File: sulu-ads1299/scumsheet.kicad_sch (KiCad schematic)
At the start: 16 parts, among them J11 through_hole, J16 through_hole, J17 through_hole, J20 through_hole, J4 through_hole, J5 through_hole, J6 through_hole, J8 through_hole, U5 scum3

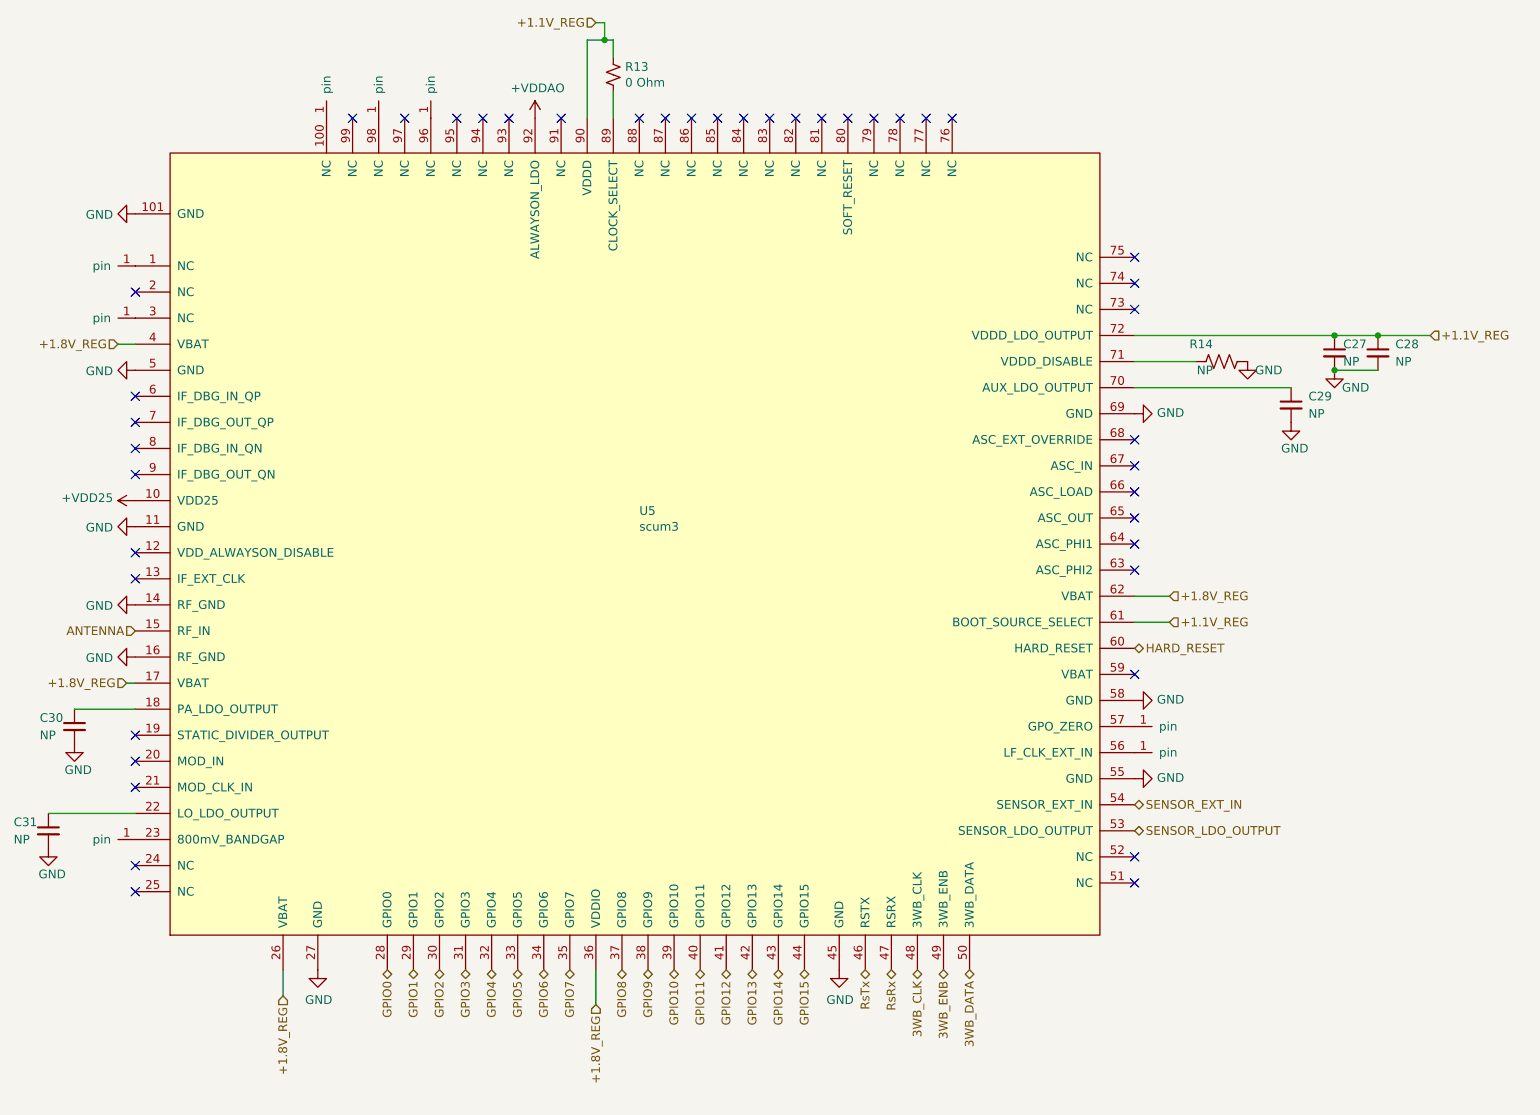
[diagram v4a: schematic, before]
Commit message: Updated connector boards and Sulu-ADS1299 schematic
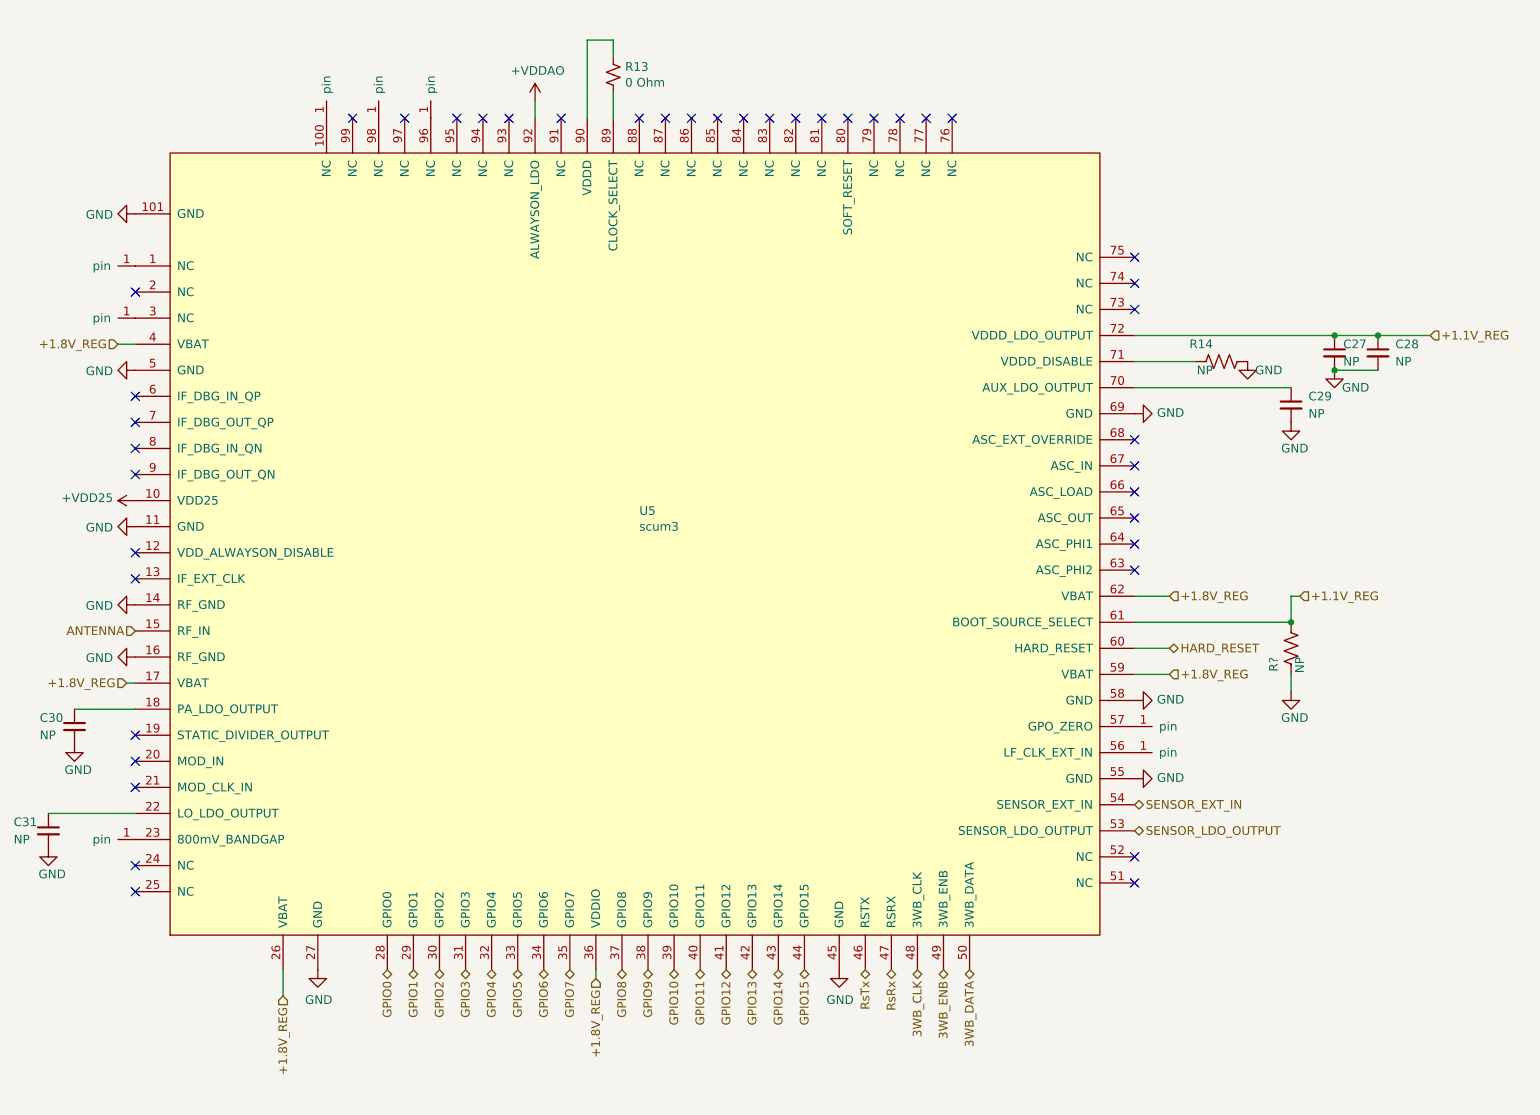
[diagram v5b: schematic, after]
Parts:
- added R?: NP, Resistor_SMD:R_0402_1005Metric, symbol Device:R_US
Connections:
- net +1.1V_REG: now also R?.2; no longer R13.1, U5.90 (VDDD)
- net +1.8V_REG: now also U5.59 (VBAT)
- net GND: now also R?.1
- new net: R13.1, U5.90 (VDDD)
- no-connect marks 43 -> 42
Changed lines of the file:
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@@
   (junction (at 245.11 60.96) (diameter 0) (color 0 0 0 0)
   )
+  (junction (at 232.41 102.87) (diameter 0) (color 0 0 0 0)
+  )
   (junction (at 238.76 60.96) (diameter 0) (color 0 0 0 0)
-  )
-  (junction (at 132.08 17.78) (diameter 0) (color 0 0 0 0)
   )
   (junction (at 238.76 66.04) (diameter 0) (color 0 0 0 0)
@@
   (no_connect (at 179.07 29.21))
   (no_connect (at 95.25 29.21))
-  (no_connect (at 209.55 110.49))
   (no_connect (at 63.5 142.24))
   (no_connect (at 209.55 57.15))
@@
   (no_connect (at 144.78 29.21))
   (no_connect (at 118.11 29.21))
+  (wire (pts (xy 233.68 99.06) (xy 232.41 99.06))
+    (stroke (width 0) (type default) (color 0 0 0 0))
+  )
   (wire (pts (xy 209.55 64.77) (xy 218.44 64.77))
     (stroke (width 0) (type default) (color 0 0 0 0))
@@
     (stroke (width 0) (type default) (color 0 0 0 0))
   )
-  (wire (pts (xy 130.81 15.24) (xy 132.08 15.24))
-    (stroke (width 0) (type default) (color 0 0 0 0))
-  )
   (wire (pts (xy 62.23 111.76) (xy 63.5 111.76))
     (stroke (width 0) (type default) (color 0 0 0 0))
   )
-  (wire (pts (xy 133.35 17.78) (xy 132.08 17.78))
-    (stroke (width 0) (type default) (color 0 0 0 0))
-  )
   (wire (pts (xy 133.35 17.78) (xy 133.35 20.32))
     (stroke (width 0) (type default) (color 0 0 0 0))
@@
     (stroke (width 0) (type default) (color 0 0 0 0))
   )
+  (wire (pts (xy 121.92 26.67) (xy 121.92 29.21))
+    (stroke (width 0) (type default) (color 0 0 0 0))
+  )
+  (wire (pts (xy 232.41 99.06) (xy 232.41 102.87))
+    (stroke (width 0) (type default) (color 0 0 0 0))
+  )
   (wire (pts (xy 50.8 130.81) (xy 63.5 130.81))
     (stroke (width 0) (type default) (color 0 0 0 0))
   )
-  (wire (pts (xy 209.55 102.87) (xy 214.63 102.87))
+  (wire (pts (xy 209.55 102.87) (xy 232.41 102.87))
+    (stroke (width 0) (type default) (color 0 0 0 0))
+  )
+  (wire (pts (xy 232.41 110.49) (xy 232.41 113.03))
     (stroke (width 0) (type default) (color 0 0 0 0))
   )
@@
     (stroke (width 0) (type default) (color 0 0 0 0))
   )
-  (wire (pts (xy 130.81 153.67) (xy 130.81 158.75))
+  (wire (pts (xy 130.81 153.67) (xy 130.81 154.94))
     (stroke (width 0) (type default) (color 0 0 0 0))
   )
@@
     (stroke (width 0) (type default) (color 0 0 0 0))
   )
+  (wire (pts (xy 209.55 110.49) (xy 214.63 110.49))
+    (stroke (width 0) (type default) (color 0 0 0 0))
+  )
   (wire (pts (xy 60.96 62.23) (xy 63.5 62.23))
     (stroke (width 0) (type default) (color 0 0 0 0))
   )
+  (wire (pts (xy 214.63 106.68) (xy 209.55 106.68))
+    (stroke (width 0) (type default) (color 0 0 0 0))
+  )
   (wire (pts (xy 129.54 29.21) (xy 129.54 17.78))
     (stroke (width 0) (type default) (color 0 0 0 0))
@@
     (stroke (width 0) (type default) (color 0 0 0 0))
   )
-  (wire (pts (xy 132.08 15.24) (xy 132.08 17.78))
-    (stroke (width 0) (type default) (color 0 0 0 0))
-  )
-  (wire (pts (xy 132.08 17.78) (xy 129.54 17.78))
+  (wire (pts (xy 129.54 17.78) (xy 133.35 17.78))
     (stroke (width 0) (type default) (color 0 0 0 0))
   )
@@
     (effects (font (size 1.27 1.27)) (justify right))
   )
-  (hierarchical_label "+1.8V_REG" (shape input) (at 130.81 158.75 270)
+  (hierarchical_label "+1.8V_REG" (shape input) (at 130.81 154.94 270)
     (effects (font (size 1.27 1.27)) (justify right))
   )
@@
     (effects (font (size 1.27 1.27)) (justify right))
   )
-  (hierarchical_label "HARD_RESET" (shape bidirectional) (at 209.55 106.68 0)
+  (hierarchical_label "HARD_RESET" (shape bidirectional) (at 214.63 106.68 0)
     (effects (font (size 1.27 1.27)) (justify left))
   )
@@
     (effects (font (size 1.27 1.27)) (justify right))
   )
+  (hierarchical_label "+1.1V_REG" (shape input) (at 233.68 99.06 0)
+    (effects (font (size 1.27 1.27)) (justify left))
+  )
   (hierarchical_label "3WB_DATA" (shape bidirectional) (at 185.42 153.67 270)
     (effects (font (size 1.27 1.27)) (justify right))
@@
     (effects (font (size 1.27 1.27)) (justify left))
   )
-  (hierarchical_label "+1.1V_REG" (shape input) (at 130.81 15.24 180)
-    (effects (font (size 1.27 1.27)) (justify right))
-  )
   (hierarchical_label "GPIO11" (shape bidirectional) (at 146.05 153.67 270)
     (effects (font (size 1.27 1.27)) (justify right))
@@
     (effects (font (size 1.27 1.27)) (justify left))
   )
-  (hierarchical_label "+1.1V_REG" (shape input) (at 214.63 102.87 0)
+  (hierarchical_label "+1.8V_REG" (shape input) (at 214.63 110.49 0)
     (effects (font (size 1.27 1.27)) (justify left))
   )
@@
     (pin "99")
   )
+  (symbol (lib_id "power:GND") (at 232.41 113.03 0) (unit 1)
+    (in_bom yes) (on_board yes)
+    (property "Reference" "#PWR?" (id 0) (at 232.41 119.38 0)
+      (effects (font (size 1.27 1.27)) hide)
+    )
+    (property "Value" "GND" (id 1) (at 234.95 116.84 0)
+      (effects (font (size 1.27 1.27)) (justify right))
+    )
+    (property "Footprint" "" (id 2) (at 232.41 113.03 0)
+      (effects (font (size 1.27 1.27)) hide)
+    )
+    (property "Datasheet" "" (id 3) (at 232.41 113.03 0)
+      (effects (font (size 1.27 1.27)) hide)
+    )
+    (pin "1")
+  )
   (symbol (lib_id "power:GND") (at 209.55 72.39 90) (unit 1)
     (in_bom yes) (on_board yes)
@@
     (pin "1")
   )
-  (symbol (lib_id "draft1library:+VDDAO") (at 121.92 29.21 0) (unit 1)
-    (in_bom yes) (on_board yes)
-    (property "Reference" "#PWR059" (id 0) (at 121.92 33.02 0)
-      (effects (font (size 1.27 1.27)) hide)
-    )
-    (property "Value" "+VDDAO" (id 1) (at 122.301 24.8158 0))
-    (property "Footprint" "" (id 2) (at 121.92 29.21 0)
-      (effects (font (size 1.27 1.27)) hide)
-    )
-    (property "Datasheet" "" (id 3) (at 121.92 29.21 0)
+  (symbol (lib_id "draft1library:+VDDAO") (at 121.92 26.67 0) (unit 1)
+    (in_bom yes) (on_board yes)
+    (property "Reference" "#PWR059" (id 0) (at 121.92 30.48 0)
+      (effects (font (size 1.27 1.27)) hide)
+    )
+    (property "Value" "+VDDAO" (id 1) (at 122.301 22.2758 0))
+    (property "Footprint" "" (id 2) (at 121.92 26.67 0)
+      (effects (font (size 1.27 1.27)) hide)
+    )
+    (property "Datasheet" "" (id 3) (at 121.92 26.67 0)
       (effects (font (size 1.27 1.27)) hide)
     )
@@
     (pin "1")
   )
+  (symbol (lib_id "Device:R_US") (at 232.41 106.68 180) (unit 1)
+    (in_bom yes) (on_board yes)
+    (property "Reference" "R?" (id 0) (at 229.87 107.95 90)
+      (effects (font (size 1.27 1.27)) (justify left))
+    )
+    (property "Value" "NP" (id 1) (at 233.68 107.95 90)
+      (effects (font (size 1.27 1.27)) (justify left))
+    )
+    (property "Footprint" "Resistor_SMD:R_0402_1005Metric" (id 2) (at 231.394 106.426 90)
+      (effects (font (size 1.27 1.27)) hide)
+    )
+    (property "Datasheet" "~" (id 3) (at 232.41 106.68 0)
+      (effects (font (size 1.27 1.27)) hide)
+    )
+    (pin "1")
+    (pin "2")
+  )
   (symbol (lib_id "draft1library:through_hole") (at 63.5 58.42 180) (unit 1)

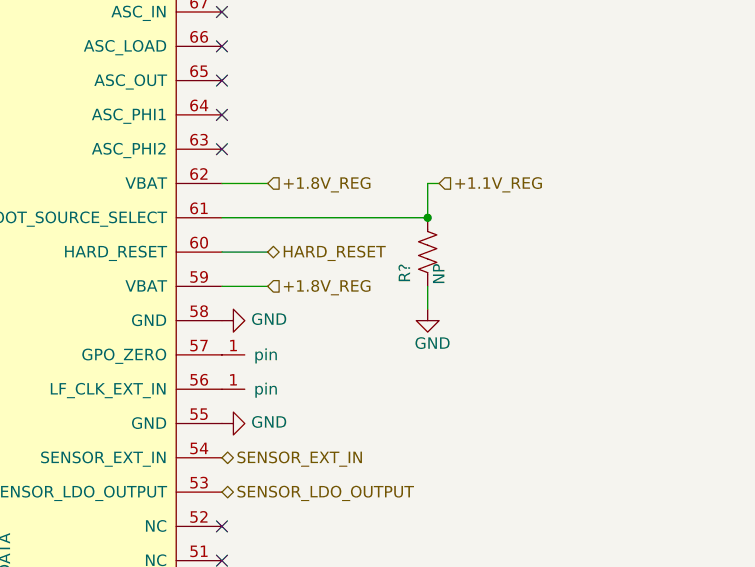
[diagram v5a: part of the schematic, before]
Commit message: Sulu-ADS1299 rev 3 fixed gpios, debug connector, two regulators
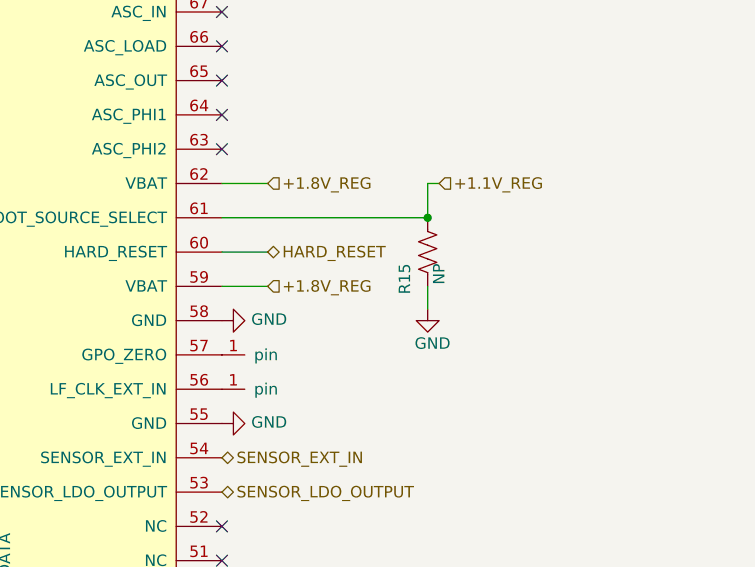
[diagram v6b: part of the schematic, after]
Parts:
- gave numbers to parts that had none: 1
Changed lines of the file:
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@@
   (symbol (lib_id "power:GND") (at 232.41 113.03 0) (unit 1)
     (in_bom yes) (on_board yes)
-    (property "Reference" "#PWR?" (id 0) (at 232.41 119.38 0)
+    (property "Reference" "#PWR01" (id 0) (at 232.41 119.38 0)
       (effects (font (size 1.27 1.27)) hide)
     )
@@
   (symbol (lib_id "Device:R_US") (at 232.41 106.68 180) (unit 1)
     (in_bom yes) (on_board yes)
-    (property "Reference" "R?" (id 0) (at 229.87 107.95 90)
+    (property "Reference" "R15" (id 0) (at 229.87 107.95 90)
       (effects (font (size 1.27 1.27)) (justify left))
     )
